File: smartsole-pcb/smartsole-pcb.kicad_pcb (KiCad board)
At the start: 2 copper layers, 24 x 22.5 mm, 38 parts, among them U1 NINA-B306-00B, U2 BQ25185DLHR, U3 BMI270, U4 MPR121QR2

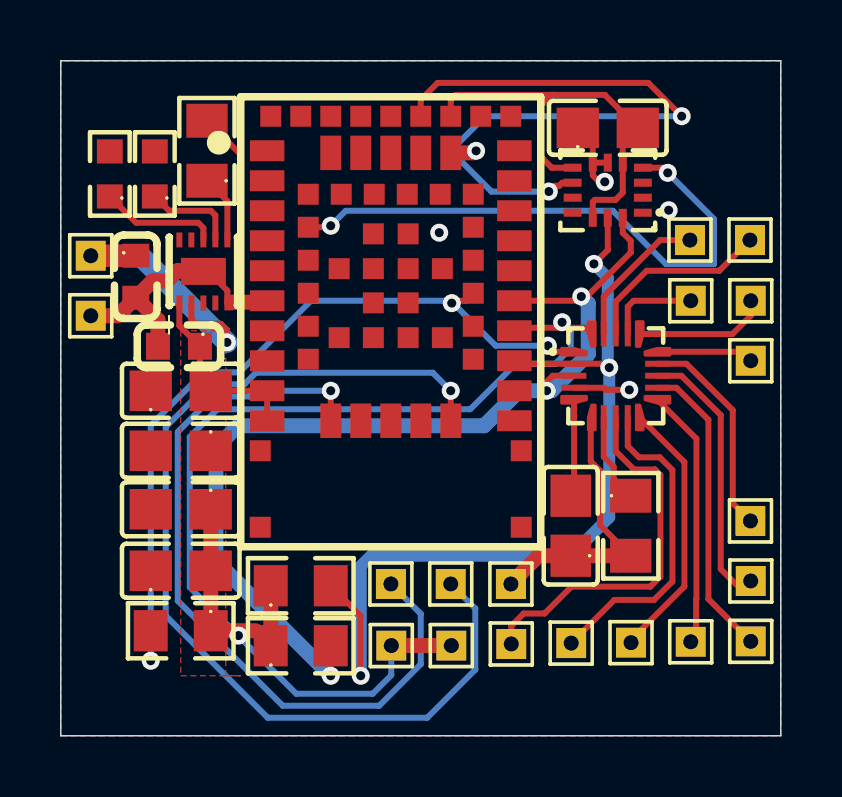
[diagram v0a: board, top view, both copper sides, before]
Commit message: added more ground vias to create faster return paths
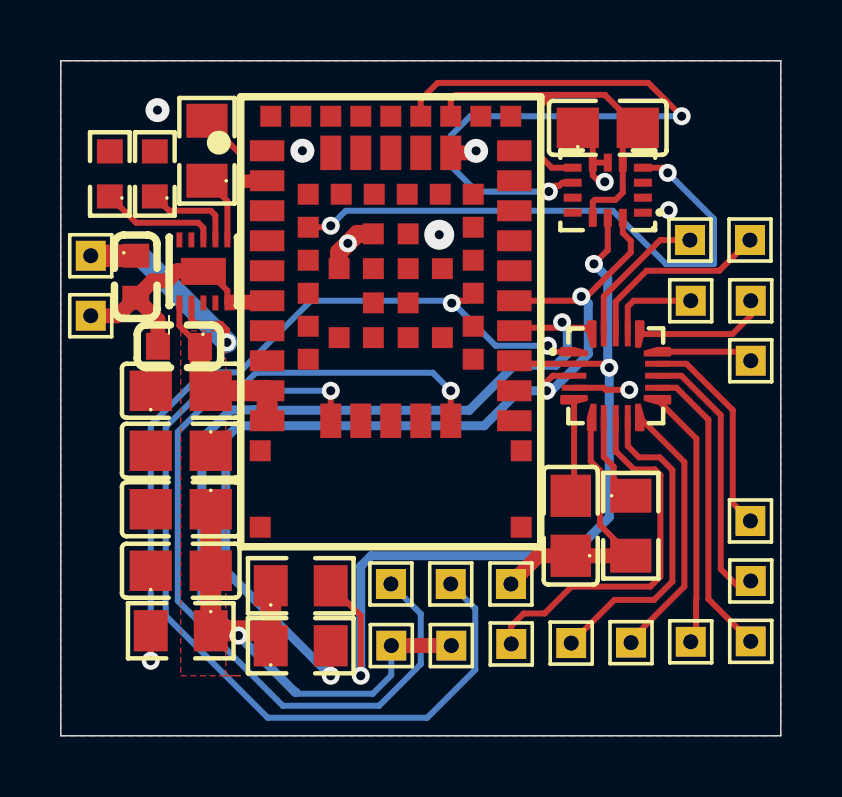
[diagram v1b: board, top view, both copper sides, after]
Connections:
- U1 pad 2: unconnected-(U1-GPIO_2-Pad2) -> GND
- U1 pad 3: unconnected-(U1-GPIO_3-Pad3) -> GND
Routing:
- net GND: track 30.6 -> 33.5 mm, vias 5 -> 8
- net /50: track 22.7 -> 23.5 mm

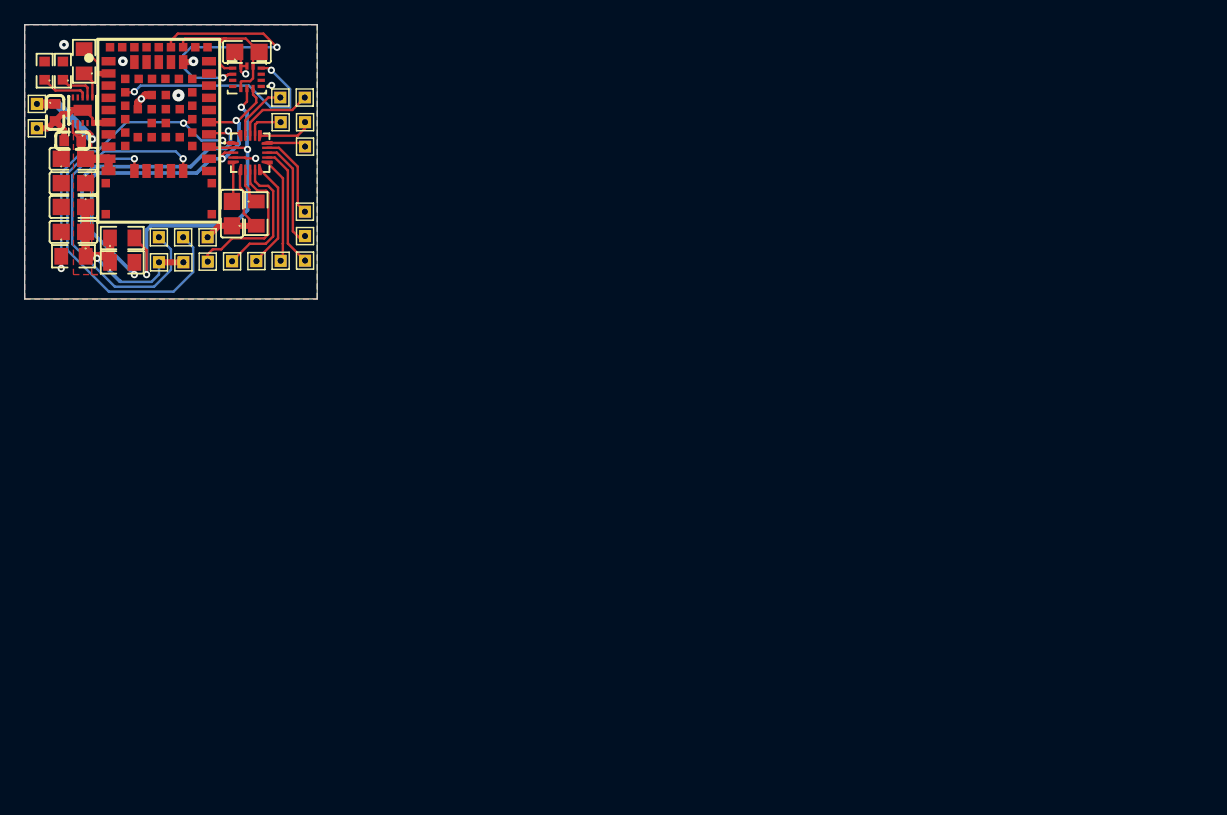
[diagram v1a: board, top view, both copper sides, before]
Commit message: began work on V1.3 - antenna moved to board edge, better GND plane, and better decoupling capacitor placement
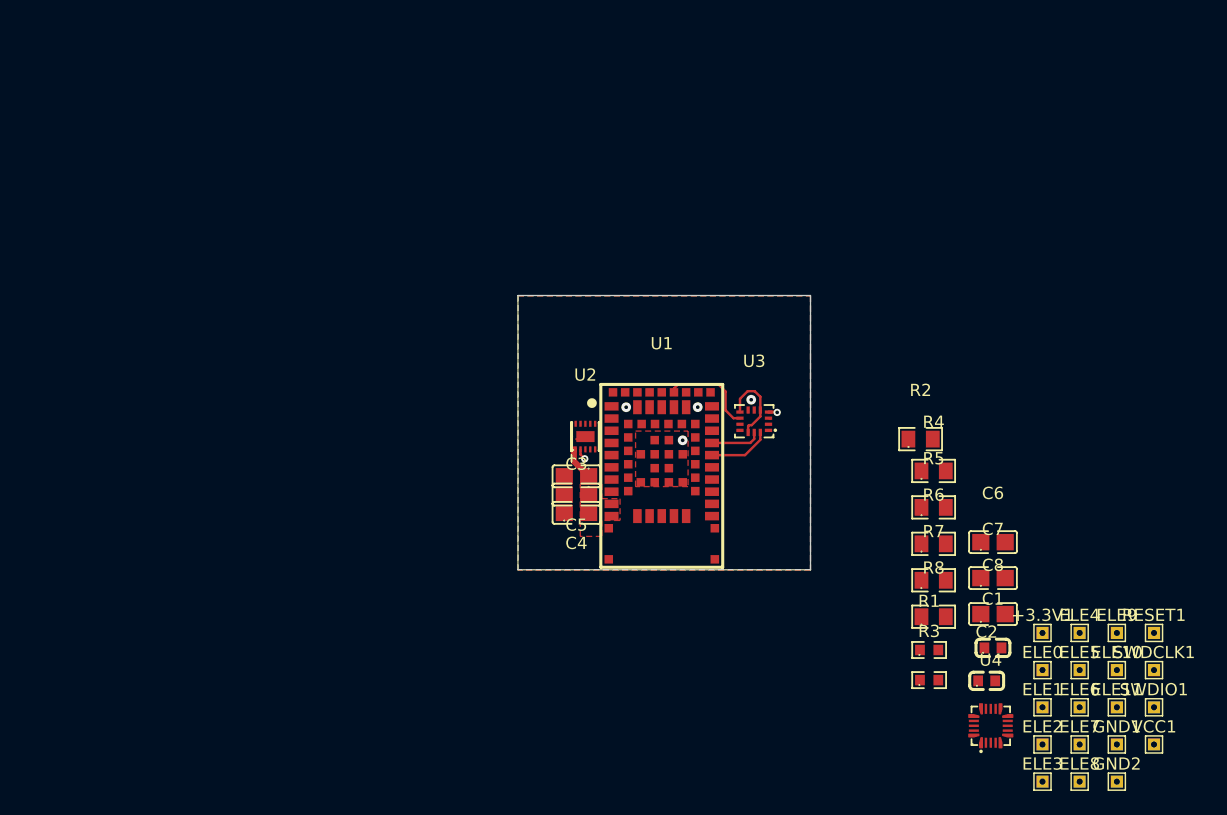
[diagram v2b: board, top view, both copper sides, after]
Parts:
- added R8: 10k, easyeda2kicad:R0805, F.Cu at (156.6, 99.6)
- moved VCC1 105.6 mm to (174.7, 110.0)
- moved GND2 103.6 mm to (171.6, 113.1)
- moved C2 89.5 mm to (160.9, 104.8), turned to 0 degrees
- moved SWDCLK1 89.0 mm to (174.7, 104.0), turned to 0 degrees
- moved SWDIO1 88.5 mm to (174.7, 107.0), turned to 0 degrees
- moved R3 88.1 mm to (156.2, 104.8), turned to 0 degrees
- moved C1 86.2 mm to (161.4, 102.1), turned to 0 degrees
- moved R1 85.5 mm to (156.2, 102.3), turned to 0 degrees
- moved GND1 85.4 mm to (171.6, 110.0), turned to 0 degrees
- moved RESET1 85.2 mm to (174.7, 100.9), turned to 0 degrees
- moved ELE11 84.9 mm to (171.6, 107.0)
- moved ELE8 83.5 mm to (168.6, 113.1)
- moved C7 82.9 mm to (161.4, 96.4)
- moved ELE10 81.5 mm to (171.6, 104.0)
- moved ELE9 80.4 mm to (171.6, 100.9)
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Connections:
- RESET1 pad 1: /+3.3V -> /RESET
- U1 pad 18: /SCL -> unconnected-(U1-GPIO_18-Pad18)
- U1 pad 19: /+3.3V -> /RESET
- U1 pad 20: /SDA -> unconnected-(U1-GPIO_20-Pad20)
- U1 pad 21: unconnected-(U1-GPIO_21-Pad21) -> /SDA
- U1 pad 22: unconnected-(U1-GPIO_22-Pad22) -> /SCL
- U1 pad 57: unconnected-(U1-Pad57) -> GND
- U1 pad 58: unconnected-(U1-Pad58) -> GND
- U1 pad 59: unconnected-(U1-Pad59) -> GND
- U1 pad 60: unconnected-(U1-Pad60) -> GND
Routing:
- net /+3.3V: track 48.8 -> 3.59 mm, vias 2 -> 0
- net Net-(SWDIO1-Pin_1): track 33.4 -> 0.00 mm, vias 1 -> 0
- net GND: track 33.5 -> 0.30 mm, vias 8 -> 4
- net /SDA: track 33.0 -> 5.09 mm, vias 3 -> 0
- net /IRQ: track 26.5 -> 0.00 mm, vias 3 -> 0
- net /SCL: track 29.9 -> 4.14 mm, vias 3 -> 0
- net Net-(SWDCLK1-Pin_1): track 25.5 -> 0.00 mm, vias 1 -> 0
- net /32: track 19.1 -> 0.68 mm, vias 2 -> 1
- net /50: track 23.5 -> 7.91 mm, vias 2 -> 0
- net Net-(ELE0-Pin_1): track 12.6 -> 0.00 mm
- net Net-(ELE1-Pin_1): track 10.7 -> 0.00 mm
- net Net-(ELE4-Pin_1): track 10.1 -> 0.00 mm
- net Net-(ELE2-Pin_1): track 8.86 -> 0.00 mm
- net Net-(ELE5-Pin_1): track 8.71 -> 0.00 mm
- net Net-(ELE3-Pin_1): track 8.68 -> 0.00 mm
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
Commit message: V1.3 - slightly smaller
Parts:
- moved SWDIO1 60.3 mm to (124.6, 73.3)
- moved SWDCLK1 56.7 mm to (124.6, 77.4)
- moved GND1 56.5 mm to (128.6, 73.4)
- moved RESET1 56.2 mm to (124.6, 75.4)
- moved ELE11 53.8 mm to (124.5, 80.9), turned to 180 degrees
- moved +3.3V1 47.7 mm to (126.6, 73.4)
- moved ELE3 47.5 mm to (124.6, 89.0), turned to 180 degrees
- moved ELE2 47.0 mm to (124.6, 87.0), turned to 180 degrees
- moved ELE1 46.5 mm to (124.6, 85.0), turned to 180 degrees
- moved ELE0 46.0 mm to (124.5, 82.9), turned to 180 degrees
- moved ELE5 45.3 mm to (124.5, 93.0), turned to 180 degrees
- moved ELE4 45.1 mm to (124.5, 91.0), turned to 180 degrees
- moved BAT_IN1 37.8 mm to (144.0, 88.0), turned to 180 degrees
- moved R8 36.2 mm to (128.8, 76.3)
- moved GND2 36.0 mm to (144.0, 90.0), turned to 180 degrees
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- renumbered VCC1 to BAT_IN1
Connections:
- U1 pad 13: unconnected-(U1-ANT-Pad13) -> GND
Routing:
- net /+3.3V: track 3.59 -> 57.4 mm, vias 0 -> 3
- net Net-(ELE11-Pin_1): track 0.00 -> 32.4 mm, vias 0 -> 1
- net /SCL: track 4.14 -> 34.5 mm, vias 0 -> 3
- net /IRQ: track 0.00 -> 28.7 mm, vias 0 -> 3
- net /SDA: track 5.09 -> 27.5 mm, vias 0 -> 2
- net Net-(SWDCLK1-Pin_1): track 0.00 -> 15.4 mm, vias 0 -> 1
- net /32: track 0.68 -> 13.8 mm, vias 1 -> 2
- net /RESET: track 0.00 -> 12.9 mm
- net Net-(ELE0-Pin_1): track 0.00 -> 12.6 mm
- net Net-(ELE1-Pin_1): track 0.00 -> 11.0 mm
- net Net-(SWDIO1-Pin_1): track 0.00 -> 11.0 mm, vias 0 -> 1
- net Net-(ELE10-Pin_1): track 0.00 -> 10.4 mm
- net Net-(ELE2-Pin_1): track 0.00 -> 9.31 mm
- net Net-(ELE9-Pin_1): track 0.00 -> 9.10 mm
- net Net-(ELE5-Pin_1): track 0.00 -> 9.08 mm
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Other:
- board size 24 x 22.5 mm -> 22.9 x 22.5 mm
